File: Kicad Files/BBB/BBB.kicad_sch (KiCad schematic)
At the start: 23 parts, among them J1 Conn_Coaxial, SW1 SW_Push, U1 STM32WBA50KGU6, Y1 NX2012_32K768, Y2 NX2016_32M

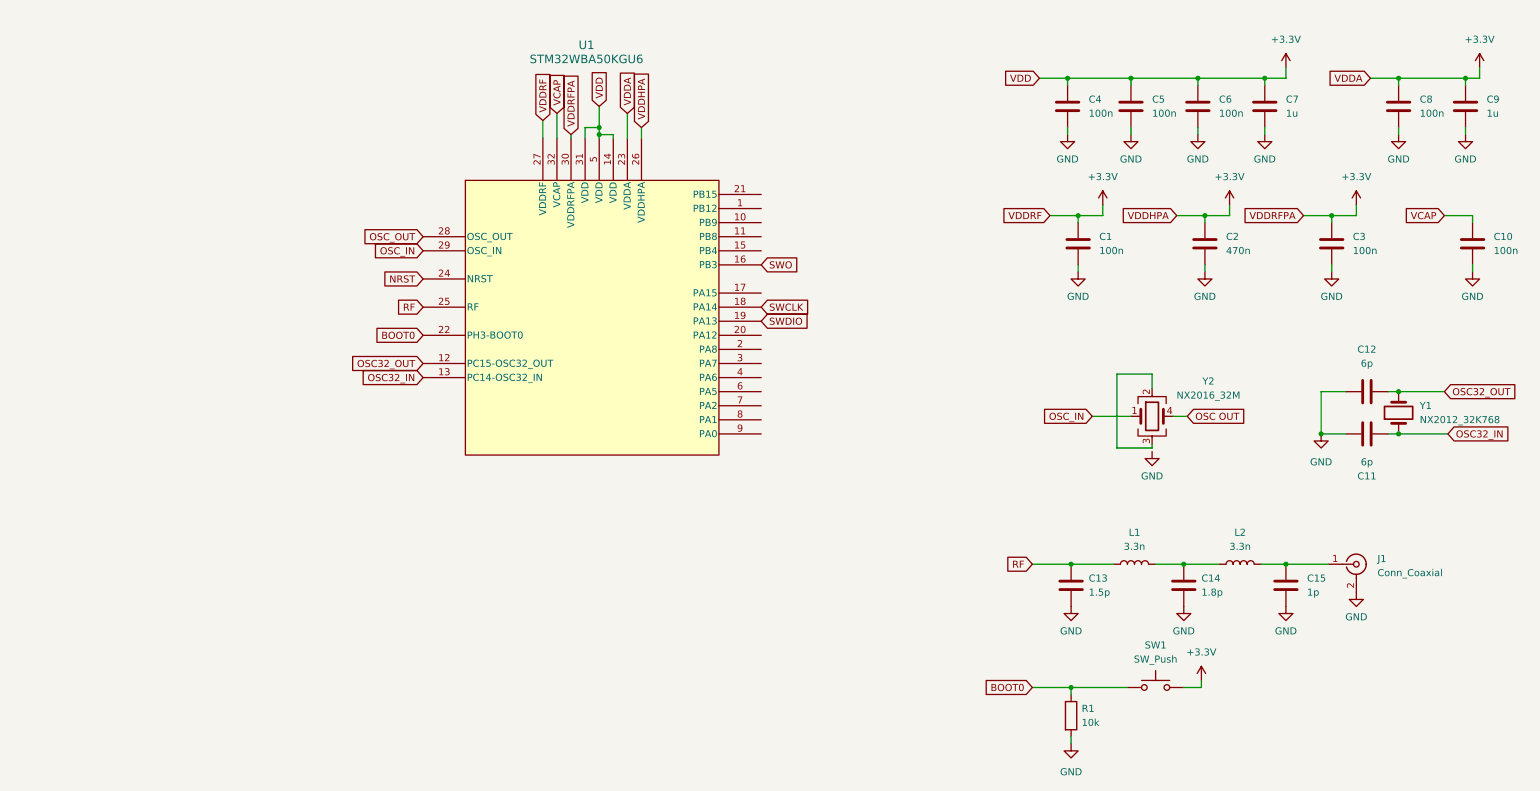
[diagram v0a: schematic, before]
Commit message: Ordering
Added labeling to the BBB

Co-Authored-By: fallencoffee <180005411+fallencoffee@users.noreply.github.com>
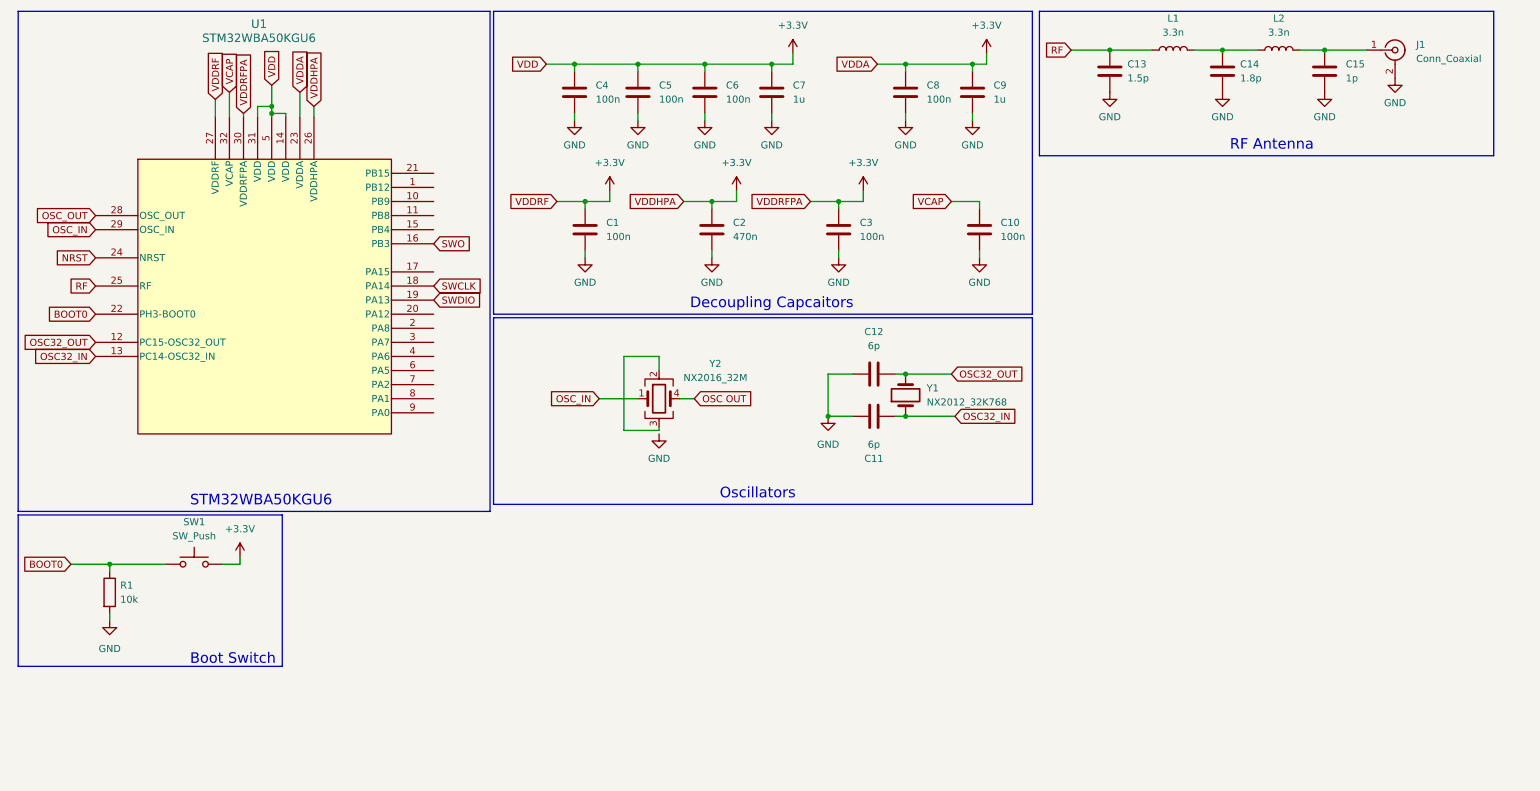
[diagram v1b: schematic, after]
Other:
- note added: "Boot Switch"
- note added: "Decoupling Capcaitors"
- note added: "Oscillators"
- note added: "RF Antenna"
- note added: "STM32WBA50KGU6"
- moved on the sheet: C1, C10, C11, C12, C13, C14, C15, C2, C3, C4, C5, C6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

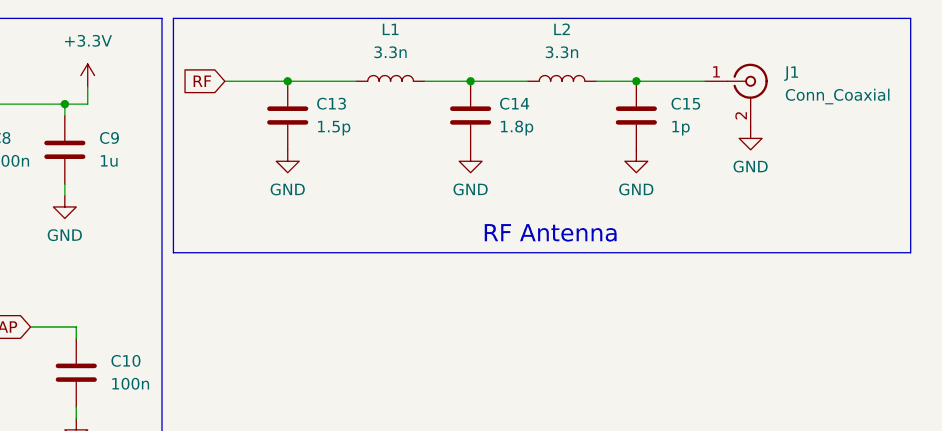
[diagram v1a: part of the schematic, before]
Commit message: Antenna
Added W3008 antenna to BBB schematic

Co-Authored-By: fallencoffee <180005411+fallencoffee@users.noreply.github.com>
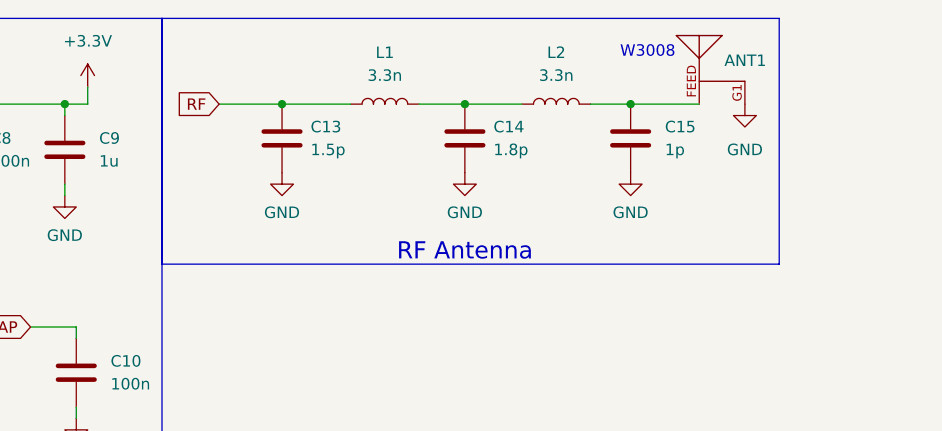
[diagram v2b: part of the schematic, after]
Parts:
- removed J1: Conn_Coaxial, symbol Connector:Conn_Coaxial
- added ANT1: W3008, W3008:ANTENNA_W3008, symbol W3008:W3008
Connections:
- net GND: now also ANT1.G1
- net at C15.1, L2.2: now also ANT1.FEED
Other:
- note added: "W3008"
- moved on the sheet: C13, C14, C15, L1, L2
